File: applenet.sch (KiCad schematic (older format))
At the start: 112 parts, among them J1 6PIN, P1 LISA_BUS, T1 157-0019, T2 157-0020, Y1 Crystal

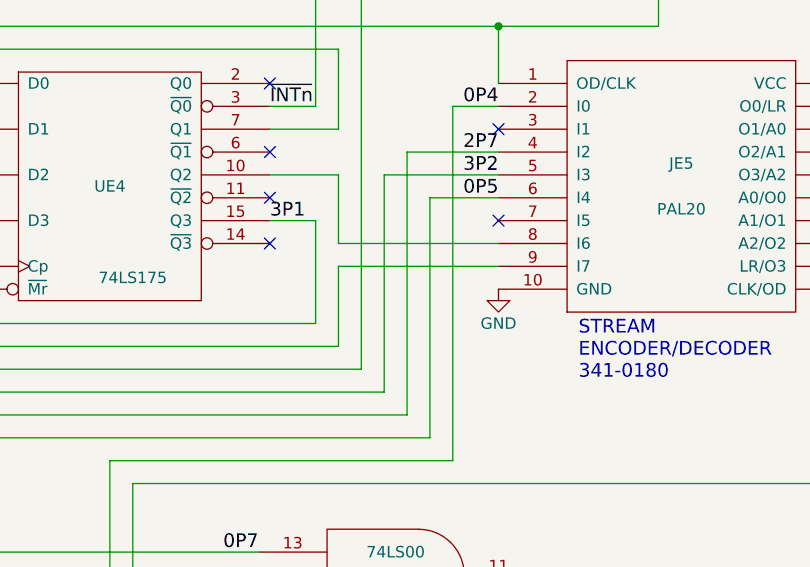
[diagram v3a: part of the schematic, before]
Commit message: Correct connections between UE4 and UE5
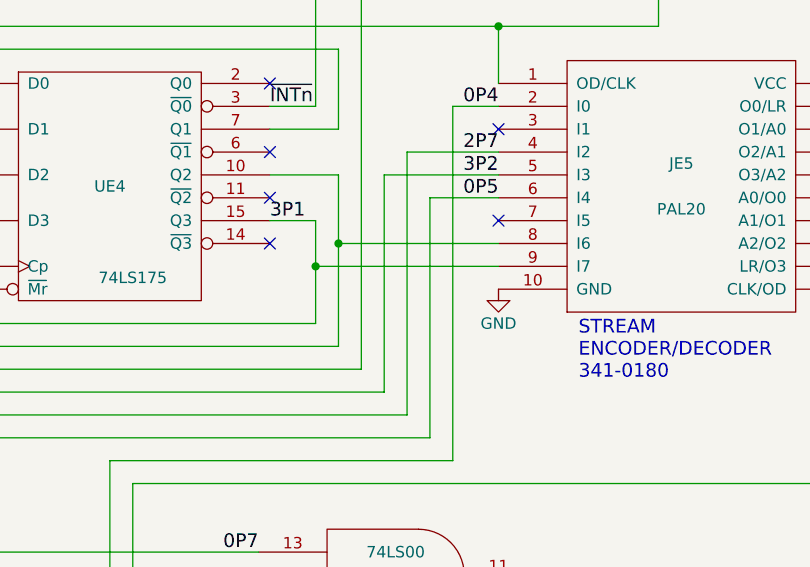
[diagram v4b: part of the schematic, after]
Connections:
- net 3P1: now also JE5.9 (I7)
- net at JE5.8 (I6), UE4.10 (Q2): now also UE4.13 (D3)
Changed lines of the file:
@@
 Sheet 1 1
 Title "Inferred schematic for the AppleNet network adaptor for Lisa"
-Date "2020-07-24"
-Rev "003 (DRAFT!)"
+Date "2020-08-10"
+Rev "004 (DRAFT!)"
 Comp ""
 Comment1 "London"
@@
 	17100 1300 17100 2150
 Wire Wire Line
-	18800 3300 18800 2950
-Wire Wire Line
-	18800 2950 19500 2950
+	18800 3300 18800 2850
 Wire Wire Line
 	16900 2950 16900 1900
@@
 Connection ~ 16400 7050
 Wire Wire Line
-	18700 2750 18700 3200
+	18700 2750 18700 2950
 Wire Wire Line
 	18700 3200 16700 3200
@@
 Wire Wire Line
 	3700 15900 3800 15900
+Connection ~ 18800 2850
+Wire Wire Line
+	19500 2950 18700 2950
 Wire Bus Line
 	20850 5950 20850 7600
@@
 Wire Bus Line
 	10400 5150 10400 10850
+Connection ~ 18700 2950
+Wire Wire Line
+	18700 2950 18700 3200
 $EndSCHEMATC
